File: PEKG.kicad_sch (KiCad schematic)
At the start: 57 parts, among them J1 USB_C_Receptacle, J2 Klema, J3 Klema, U1 TL072, U10 74LVC1G125, U11 74LVC1G125, U2 TL072, U3 TL072, U4 74LVC2G74, U5 TS5A63157DBV, U6 TS5A63157DBV, U7 TS5A63157DBV, U9 74LVC1G125

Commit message: Changed input opamps to NCS.
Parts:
- removed U1, U2: TL072, Package_SO:SOIC-8_3.9x4.9mm_P1.27mm, symbol Amplifier_Operational:TL072
- added U12, U8: NCS21802DMR2G, Package_SO:OnSemi_Micro8, symbol voltmeter_lib:NCS21802DMR2G
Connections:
- net BUFFERS_OUTPUT: now also U12.1
- net COMMON_INPUT_LEVEL: now also U12.6 (-)
- net GND: now also J1.A5 (CC1), J1.B5 (CC2), U12.5 (+)
- net VCC: now also U12.8 (V+), U8.8 (V+)
- net VEE: now also U12.4 (V-), U8.4 (V-)
- net at R7.1, R8.2: now also U12.2 (-)
- net at R6.1, R9.2: now also U12.3 (+)
- net at D2.3 (K), R11.1: now also U8.5 (+)
- net at C15.1, R2.1, R3.2: now also U8.6 (-)
- net at C15.2, R3.1, R5.1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: now also U8.7
- net at C16.2, R1.1, R2.2: now also U8.2 (-)
- net at C16.1, R1.2, R4.2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: now also U8.1
- net at D1.3 (K), R10.1: now also U8.3 (+)
- net at R13.1: now also U12.7
- no-connect marks 15 -> 13
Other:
- note added: "Implementiraj neki invertujući prekidački konverter za -5V rail. Možda switched capacitor."
- note added: "https://www.usb.org/sites/default/files/USB%20Type-C%20Spec%20R2.0%20-%20August%202019.pdf"

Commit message: Added stages, todos.
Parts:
- removed U3: TL072, Package_SO:SOIC-8_3.9x4.9mm_P1.27mm, symbol Amplifier_Operational:TL072
- added C21, C22, C23: 10u, Capacitor_SMD:C_0603_1608Metric_Pad1.08x0.95mm_HandSolder, symbol Device:C
- added C24, C25: 10n, Capacitor_SMD:C_0603_1608Metric_Pad1.08x0.95mm_HandSolder, symbol Device:C
- added C26: 100n, Capacitor_SMD:C_0603_1608Metric_Pad1.08x0.95mm_HandSolder, symbol Device:C
- added C27: 1u, Capacitor_SMD:C_0603_1608Metric_Pad1.08x0.95mm_HandSolder, symbol Device:C
- added R17, R24: 100k, Resistor_SMD:R_0603_1608Metric_Pad0.98x0.95mm_HandSolder, symbol Device:R
- added R25: 190k, Resistor_SMD:R_0603_1608Metric_Pad0.98x0.95mm_HandSolder, symbol Device:R
- added R26, R27, R30, R31: 10k, Resistor_SMD:R_0603_1608Metric_Pad0.98x0.95mm_HandSolder, symbol Device:R
- added R28, R29: 20k, Resistor_SMD:R_0603_1608Metric_Pad0.98x0.95mm_HandSolder, symbol Device:R
- added U13, U14: NCS21802DMR2G, Package_SO:OnSemi_Micro8, symbol voltmeter_lib:NCS21802DMR2G
- C15, C16: now not fitted
- C7: value 10u -> 100n
- R1, R3: value 1k -> 20k
- R15, R16, R18, R23: value 1k -> 100k
- R2: value 1k -> 10k
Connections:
- net COMMON_OUTPUT_LEVEL is gone; now on net DC_COMPENSATION: R9.1
- net OUTPUT is gone; now on net VCC: R18.2
- net DC_COMPENSATION: now also R16.1, C22.1, U13.1; no longer C7.1, R16.2
- net GND: now also C7.2, C26.1, R24.1; no longer R23.1
- net VCC: now also C7.1, C27.1, R28.2, U13.8 (V+), U14.8 (V+)
- net VEE: now also C26.2, C27.2, U13.4 (V-), U14.4 (V-)
- net TOP: now reaches C16.1, R1.2, R4.2, R6.2, U8.1
- net TOP: now also R15.2
- net BOTTOM: now reaches C15.2, R3.1, R5.1, R7.2, U8.7
- net BOTTOM: now also R14.2
- net at R23.2: now also C23.2, U13.6 (-); no longer R18.1
- net at R14.1: now also R16.2, C22.2, U13.2 (-); no longer C7.2
- net at R15.1: now also C21.1, R17.1, U13.3 (+); no longer R16.1
- net BUFFERS_OUTPUT renamed GAIN_5_OUTPUT
- net GAIN_5_OUTPUT: now also U14.3 (+); no longer R14.2, R15.2
- new net: C24.2, R25.2, R26.1, U14.2 (-)
- new net: R30.1, R31.1, U14.5 (+)
- new net: C25.2, R27.2, R28.1, R29.1, U14.6 (-)
- new net: R18.1, R24.2, U13.5 (+)
- new net 2.5V: C21.2, C23.1, R17.2, R23.1, R26.2, R29.2, R31.2, U13.7
- new net GAIN_100_OUTPUT: C24.1, R25.1, R30.2, U14.1
- new net LEVELED_OUTPUT: C25.1, R27.1, U14.7
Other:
- note added: "DODATI NOTCH FILTER"
- note added: "DOUBLE CHECK VREDNOSTI"
- note added: "MOŽDA DODATI JEFTINIJI OPAMP NAKOG GAIN-A"
- note added: "PRERAČUNATI PROPUSNE OPSEGE"
- note removed: "Implementiraj neki invertujući prekidački konverter za -5V rail. Možda switched capacitor."
- moved on the sheet: C10, R14

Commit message: Minor update.
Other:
- note added: "Gain to 100, changing the common mode point"
- moved on the sheet: C14, C24, C25, C26, C27, C7, J1, J2, J3, R25, R26, R27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

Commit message: Little PCB modifications.
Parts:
- removed J2, J3: Klema, TerminalBlock:TerminalBlock_MaiXu_MX126-5.0-02P_1x02_P5.00mm, symbol Connector:Screw_Terminal_01x02
- added H1, H2, H3, H4: MountingHole, MountingHole:MountingHole_3.2mm_M3_ISO14580_Pad_TopBottom, symbol Mechanical:MountingHole
- added J2: AudioJack3, PEKG:Jack_3.5mm_CUI_SJ1-3523N_Horizontal, symbol Connector_Audio:AudioJack3
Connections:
- net RIGHT_LEG_DRIVE: now also J2.T
- net NEGATIVE_INPUT renamed RIGHT_ARM
- net RIGHT_ARM: now also J2.S
- net POSITIVE_INPUT renamed LEFT_ARM
- net LEFT_ARM: now also J2.R

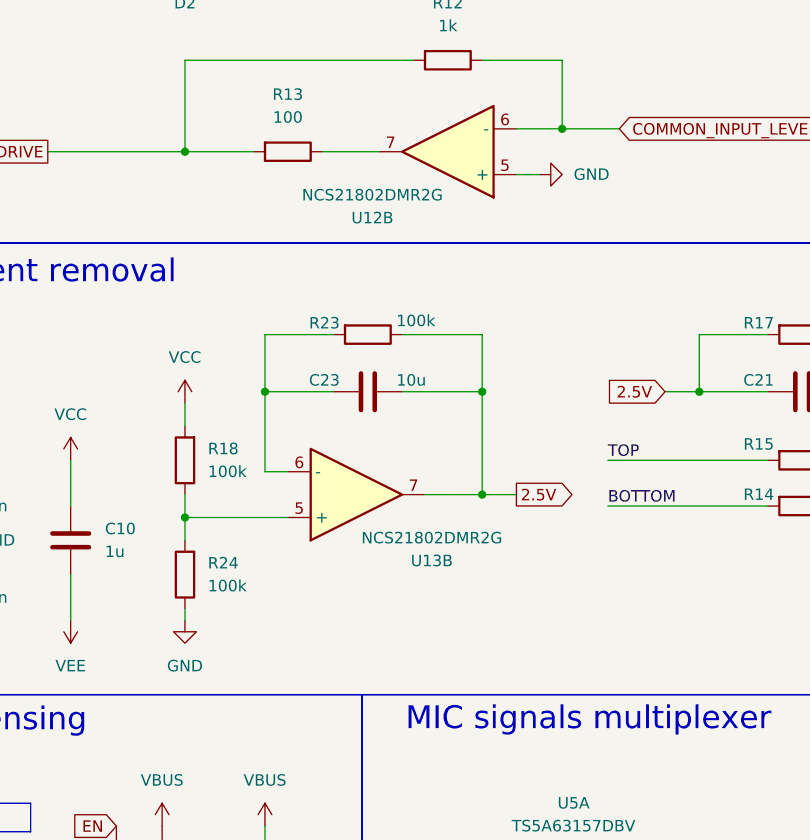
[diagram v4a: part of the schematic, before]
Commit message: Tad saner schematic.
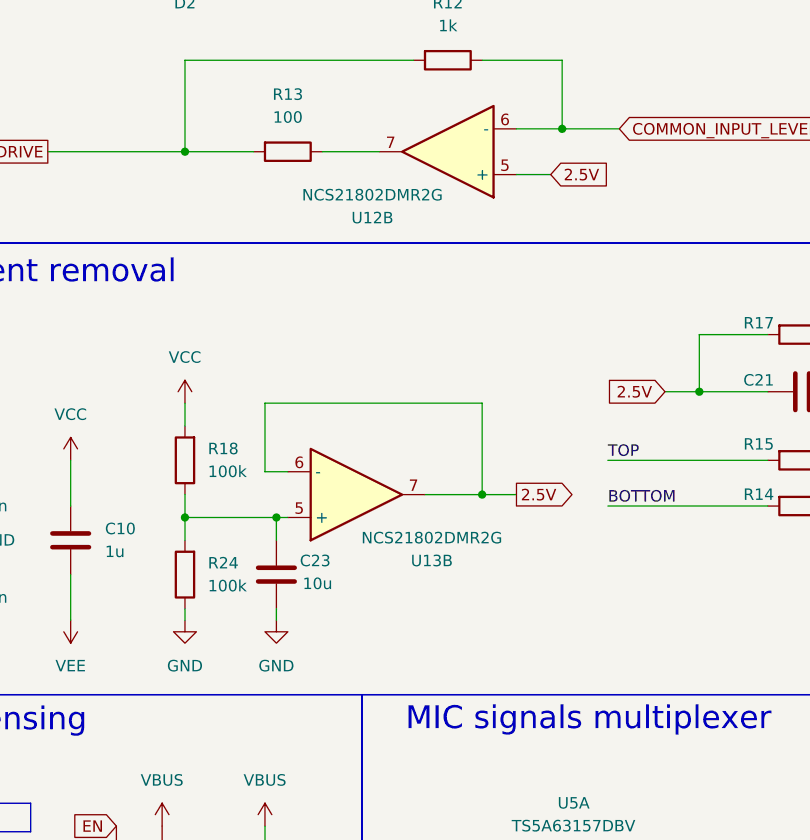
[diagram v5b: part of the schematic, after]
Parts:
- removed R23: 100k, Resistor_SMD:R_0603_1608Metric_Pad0.98x0.95mm_HandSolder, symbol Device:R
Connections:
- net 2.5V: now also U12.5 (+), U13.6 (-); no longer C23.1
- net GND: now also C23.2; no longer U12.5 (+)
- net at R18.1, R24.2, U13.5 (+): now also C23.1
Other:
- moved on the sheet: C23
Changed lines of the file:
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@@
 	)
 	(junction
-		(at 67.31 137.16)
-		(diameter 0)
-		(color 0 0 0 0)
-	)
-	(junction
 		(at 33.02 58.42)
 		(diameter 0)
@@
 	)
 	(junction
-		(at 58.42 64.77)
+		(at 68.58 151.13)
 		(diameter 0)
 		(color 0 0 0 0)
 	)
 	(junction
-		(at 82.55 64.77)
+		(at 58.42 64.77)
 		(diameter 0)
 		(color 0 0 0 0)
 	)
 	(junction
-		(at 91.44 39.37)
+		(at 82.55 64.77)
 		(diameter 0)
 		(color 0 0 0 0)
 	)
 	(junction
-		(at 91.44 137.16)
+		(at 91.44 39.37)
 		(diameter 0)
 		(color 0 0 0 0)
@@
 	(wire
 		(pts
-			(xy 91.44 137.16) (xy 91.44 148.59)
-		)
-		(stroke
-			(width 0)
-			(type default)
-		)
-	)
-	(wire
-		(pts
 			(xy 133.35 259.08) (xy 133.35 260.35)
 		)
@@
 	(wire
 		(pts
-			(xy 58.42 151.13) (xy 69.85 151.13)
+			(xy 58.42 151.13) (xy 68.58 151.13)
 		)
 		(stroke
@@
 	(wire
 		(pts
-			(xy 82.55 130.81) (xy 91.44 130.81)
-		)
-		(stroke
-			(width 0)
-			(type default)
-		)
-	)
-	(wire
-		(pts
 			(xy 161.29 162.56) (xy 161.29 156.21)
 		)
@@
 	(wire
 		(pts
-			(xy 82.55 137.16) (xy 91.44 137.16)
-		)
-		(stroke
-			(width 0)
-			(type default)
-		)
-	)
-	(wire
-		(pts
 			(xy 137.16 162.56) (xy 137.16 156.21)
 		)
@@
 	(wire
 		(pts
-			(xy 148.59 251.46) (xy 148.59 252.73)
+			(xy 68.58 151.13) (xy 69.85 151.13)
 		)
 		(stroke
@@
 	(wire
 		(pts
-			(xy 265.43 91.44) (xy 259.08 91.44)
+			(xy 148.59 251.46) (xy 148.59 252.73)
 		)
 		(stroke
@@
 	(wire
 		(pts
-			(xy 95.25 107.95) (xy 100.33 107.95)
+			(xy 265.43 91.44) (xy 259.08 91.44)
 		)
 		(stroke
@@
 	(wire
 		(pts
-			(xy 67.31 130.81) (xy 67.31 137.16)
+			(xy 95.25 107.95) (xy 100.33 107.95)
 		)
 		(stroke
@@
 	(wire
 		(pts
+			(xy 68.58 161.29) (xy 68.58 162.56)
+		)
+		(stroke
+			(width 0)
+			(type default)
+		)
+	)
+	(wire
+		(pts
 			(xy 105.41 58.42) (xy 105.41 64.77)
 		)
@@
 	(wire
 		(pts
-			(xy 74.93 137.16) (xy 67.31 137.16)
-		)
-		(stroke
-			(width 0)
-			(type default)
-		)
-	)
-	(wire
-		(pts
 			(xy 166.37 93.98) (xy 166.37 99.06)
 		)
@@
 	(wire
 		(pts
-			(xy 91.44 137.16) (xy 91.44 130.81)
+			(xy 91.44 138.43) (xy 91.44 148.59)
 		)
 		(stroke
@@
 	(wire
 		(pts
-			(xy 97.79 113.03) (xy 95.25 113.03)
+			(xy 68.58 153.67) (xy 68.58 151.13)
+		)
+		(stroke
+			(width 0)
+			(type default)
+		)
+	)
+	(wire
+		(pts
+			(xy 99.06 113.03) (xy 95.25 113.03)
 		)
 		(stroke
@@
 	(wire
 		(pts
-			(xy 67.31 137.16) (xy 67.31 146.05)
+			(xy 67.31 138.43) (xy 67.31 146.05)
 		)
 		(stroke
@@
 	(wire
 		(pts
-			(xy 67.31 130.81) (xy 74.93 130.81)
+			(xy 67.31 138.43) (xy 91.44 138.43)
 		)
 		(stroke
@@
 			"pKTE03MUarV68eLF4eHh07G4wZIlS1QqlS97CA4OXrJkieTXysPJCgAAQcDRMQCAICDHAACCgBwD"
 			"AAgCcgwAIAjIMQCAICDHAACCgBwDAAgCcgwAIAjIMQCAICDHAACCgBwDAAgCcgwAIAjIMQCAICDH"
-			"AACCgBwDAAgCcgwAIAjIMQCAICDHAACC8P9FoxsOaeCU/wAAAABJRU5ErkJggg=="
+			"AACCgBwDAAgCcgwAIAjIMQCAICDHAACC8P9FoxsOaeCU/wAAAABJRU5ErkJgggAAAAAAAAAAAAAA"
+			"AAAAAAAAAAAAAAAAAAAAAAAAAAAAAAAAAAAAAAAAAAAAAAAAAAAAAAAAAAAAAAAAAAAAAAAAAAAA"
+			"AAAAAAAAAAAAAAAAAAAAAAAAAAAAAAAAAAAAAAAAAAAAAAAAAAAAAAAAAAAAAAAAAAAAAAAAAAAA"
+			"AAAAAAAAAAAAAAAAAAAAAAAAAAAAAAAAAAAAAAAAAAAAAAAAAAAAAAAAAAAAAAAAAAAAAAAAAAAA"
+			"AAAAAAAAAAAAAAAAAAAAAAAAAAAAAAAAAAAAAAAAAAAAAAAAAAAAAAAAAAAAAAAAAAAAAAAAAAAA"
+			"AAAAAAAAAAAAAAAAAAAAAAAAAAAAAAAAAAAAAAAAAAAAAAAAAAAAAAAAAAAAAAAAAAAAAAAAAAAA"
+			"AAAAAAAAAAAAAAAAAAAAAAAAAAAAAAAAAAAAAAAAAAAAAAAAAAAAAAAAAAAAAAAAAAAAAAAAAAAA"
+			"AAAAAAAAAAAAAAAAAAAAAAAAAAAAAAAAAAAAAAAAAAAAAAAAAAAAAAAAAAAAAAAAAAAAAAAAAAAA"
+			"AAAAAAAAAAAAAAAAAAAAAAAAAAAAAAAAAAAAAAAAAAAAAAAAAAAAAAAAAAAAAAAAAAAAAAAAAAAA"
+			"AAAAAAAAAAAAAAAAAAAAAAAAAAAAAAAAAAAAAAAAAAAAAAAAAAAAAAAAAAAAAAAAAAAAAAAAAAAA"
+			"AAAAAAAAAAAAAAAAAAAAAAAAAAAAAAAAAAAAAAAAAAAAAAAAAAAAAAAAAAAAAAAAAAAAAAAAAAAA"
+			"AAAAAAAAAAAAAAAAAAAAAAAAAAAAAAAAAAAAAAAAAAAAAAAAAAAAAAAAAAAAAAAAAAAAAAAAAAAA"
+			"AAAAAAAAAAAAAAAAAAAAAAAAAAAAAAAAAAAAAAAAAAAAAAAAAAAAAAAAAAAAAAAAAAAAAAAAAAAA"
+			"AAAAAAAAAAAAAAAAAAAAAAAAAAAAAAAAAAAAAAAAAAAAAAAAAAAAAAAAAAAAAAAAAAAAAAAAAAAA"
+			"AAAAAAAAAAAAAAAAAAAAAAAAAAAAAAAAAAAAAAAAAAAAAAAAAAAAAAAAAAAAAAAAAAAAAAAAAAAA"
+			"AAAAAAAAAAAAAAAAAAAAAAAAAAAAAAAAAAAAAAAAAAAAAAAAAAAAAAAAAAAAAAAAAAAAAAAAAAAA"
+			"AAAAAAAAAAAAAAAAAAAAAAAAAAAAAAAAAAAAAAAAAAAAAAAAAAAAAAAAAAAAAAAAAAAAAAAAAAAA"
+			"AAAAAAAAAAAAAAAAAAAAAAAAAAAAAAAAAAAAAAAAAAAAAAAAAAAAAAAAAAAAAAAAAAAAAAAAAAAA"
+			"AAAAAAAAAAAAAAAAAAAAAAAAAAAAAAAAAAAAAAAAAAAAAAAAAAAAAAAAAAAAAA=="
 		)
 	)
@@
 	(global_label "2.5V"
 		(shape input)
+		(at 99.06 113.03 0)
+		(fields_autoplaced yes)
+		(effects
+			(font
+				(size 1.27 1.27)
+			)
+			(justify left)
+		)
+		(property "Intersheetrefs" "${INTERSHEET_REFS}"
+			(at 106.1576 113.03 0)
+			(effects
+				(font
+					(size 1.27 1.27)
+				)
+				(justify left)
+				(hide yes)
+			)
+		)
+	)
+	(global_label "2.5V"
+		(shape input)
 		(at 217.17 80.01 180)
 		(fields_autoplaced yes)
@@
 	)
 	(symbol
-		(lib_id "Device:R")
-		(at 78.74 130.81 270)
-		(unit 1)
-		(exclude_from_sim no)
-		(in_bom yes)
-		(on_board yes)
-		(dnp no)
-		(property "Reference" "R23"
-			(at 73.914 129.54 90)
-			(effects
-				(font
-					(size 1.27 1.27)
-				)
-			)
-		)
-		(property "Value" "100k"
-			(at 84.074 129.286 90)
-			(effects
-				(font
-					(size 1.27 1.27)
-				)
-			)
-		)
-		(property "Footprint" "Resistor_SMD:R_0603_1608Metric_Pad0.98x0.95mm_HandSolder"
-			(at 78.74 129.032 90)
-			(effects
-				(font
-					(size 1.27 1.27)
-				)
-				(hide yes)
-			)
-		)
-		(property "Datasheet" "~"
-			(at 78.74 130.81 0)
-			(effects
-				(font
-					(size 1.27 1.27)
-				)
-				(hide yes)
-			)
-		)
-		(property "Description" "Resistor"
-			(at 78.74 130.81 0)
-			(effects
-				(font
-					(size 1.27 1.27)
-				)
-				(hide yes)
-			)
-		)
-		(pin "2"
-		)
-		(pin "1"
-		)
-		(instances
-			(project "PEKG"
-				(path "/6b6ace37-3aeb-4177-8f53-de4683f890d9"
-					(reference "R23")
-					(unit 1)
-				)
-			)
-		)
-	)
-	(symbol
 		(lib_id "power:VCC")
 		(at 17.78 146.05 0)
@@
 	)
 	(symbol
-		(lib_id "power:GND")
-		(at 97.79 113.03 90)
-		(unit 1)
-		(exclude_from_sim no)
-		(in_bom yes)
-		(on_board yes)
-		(dnp no)
-		(fields_autoplaced yes)
-		(property "Reference" "#PWR022"
-			(at 104.14 113.03 0)
-			(effects
-				(font
-					(size 1.27 1.27)
-				)
-				(hide yes)
-			)
-		)
-		(property "Value" "GND"
-			(at 101.6 113.0299 90)
-			(effects
-				(font
-					(size 1.27 1.27)
-				)
-				(justify right)
-			)
-		)
-		(property "Footprint" ""
-			(at 97.79 113.03 0)
-			(effects
-				(font
-					(size 1.27 1.27)
-				)
-				(hide yes)
-			)
-		)
-		(property "Datasheet" ""
-			(at 97.79 113.03 0)
-			(effects
-				(font
-					(size 1.27 1.27)
-				)
-				(hide yes)
-			)
-		)
-		(property "Description" "Power symbol creates a global label with name \"GND\" , ground"
-			(at 97.79 113.03 0)
-			(effects
-				(font
-					(size 1.27 1.27)
-				)
-				(hide yes)
-			)
-		)
-		(pin "1"
-		)
-		(instances
-			(project "EEG"
-				(path "/6b6ace37-3aeb-4177-8f53-de4683f890d9"
-					(reference "#PWR022")
-					(unit 1)
-				)
-			)
-		)
-	)
-	(symbol
 		(lib_id "power:VCC")
 		(at 66.04 29.21 270)
@@
 	(symbol
 		(lib_id "Device:C")
-		(at 78.74 137.16 270)
-		(mirror x)
+		(at 68.58 157.48 0)
+		(mirror y)
 		(unit 1)
 		(exclude_from_sim no)
@@
 		(dnp no)
 		(property "Reference" "C23"
-			(at 73.914 135.89 90)
+			(at 72.898 155.956 0)
 			(effects
 				(font
@@
 		)
 		(property "Value" "10u"
-			(at 83.566 135.89 90)
+			(at 73.152 158.496 0)
 			(effects
 				(font
@@
 		)
 		(property "Footprint" "Capacitor_SMD:C_0603_1608Metric_Pad1.08x0.95mm_HandSolder"
-			(at 74.93 136.1948 0)
+			(at 67.6148 161.29 0)
 			(effects
 				(font
@@
 		)
 		(property "Datasheet" "~"
-			(at 78.74 137.16 0)
+			(at 68.58 157.48 0)
 			(effects
 				(font
@@
 		)
 		(property "Description" "Unpolarized capacitor"
-			(at 78.74 137.16 0)
+			(at 68.58 157.48 0)
 			(effects
 				(font
@@
 					(unit 1)
 				)
+			)
+		)
+	)
+	(symbol
+		(lib_id "power:GND")
+		(at 68.58 162.56 0)
+		(unit 1)
+		(exclude_from_sim no)
+		(in_bom yes)
+		(on_board yes)
+		(dnp no)
+		(fields_autoplaced yes)
+		(property "Reference" "#PWR081"
+			(at 68.58 168.91 0)
+			(effects
+				(font
+					(size 1.27 1.27)
+				)
+				(hide yes)
+			)
+		)
+		(property "Value" "GND"
+			(at 68.58 167.64 0)
+			(effects
+				(font
+					(size 1.27 1.27)
+				)
+			)
+		)
+		(property "Footprint" ""
+			(at 68.58 162.56 0)
+			(effects
+				(font
+					(size 1.27 1.27)
+				)
+				(hide yes)
+			)
+		)
+		(property "Datasheet" ""
+			(at 68.58 162.56 0)
+			(effects
+				(font
+					(size 1.27 1.27)
+				)
+				(hide yes)
+			)
+		)
+		(property "Description" "Power symbol creates a global label with name \"GND\" , ground"
+			(at 68.58 162.56 0)
+			(effects
+				(font
+					(size 1.27 1.27)
+				)
+				(hide yes)
+			)
+		)
+		(pin "1"
+		)
+		(instances
+			(project "PEKG"
+				(path "/6b6ace37-3aeb-4177-8f53-de4683f890d9"
+					(reference "#PWR081")
+					(unit 1)
+				)

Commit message: Newwww
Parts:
- R12: value 1k -> 100k -> inf
- R13: value 100 -> 1
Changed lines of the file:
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@@
 			"AAAAAAAAAAAAAAAAAAAAAAAAAAAAAAAAAAAAAAAAAAAAAAAAAAAAAAAAAAAAAAAAAAAAAAAAAAAA"
 			"AAAAAAAAAAAAAAAAAAAAAAAAAAAAAAAAAAAAAAAAAAAAAAAAAAAAAAAAAAAAAAAAAAAAAAAAAAAA"
+			"AAAAAAAAAAAAAAAAAAAAAAAAAAAAAAAAAAAAAAAAAAAAAAAAAAAAAAAAAAAAAAAAAAAAAAAAAAAA"
+			"AAAAAAAAAAAAAAAAAAAAAAAAAAAAAAAAAAAAAAAAAAAAAAAAAAAAAAAAAAAAAAAAAAAAAAAAAAAA"
+			"AAAAAAAAAAAAAAAAAAAAAAAAAAAAAAAAAAAAAAAAAAAAAAAAAAAAAAAAAAAAAAAAAAAAAAAAAAAA"
+			"AAAAAAAAAAAAAAAAAAAAAAAAAAAAAAAAAAAAAAAAAAAAAAAAAAAAAAAAAAAAAAAAAAAAAAAAAAAA"
+			"AAAAAAAAAAAAAAAAAAAAAAAAAAAAAAAAAAAAAAAAAAAAAAAAAAAAAAAAAAAAAAAAAAAAAAAAAAAA"
+			"AAAAAAAAAAAAAAAAAAAAAAAAAAAAAAAAAAAAAAAAAAAAAAAAAAAAAAAAAAAAAAAAAAAAAAAAAAAA"
+			"AAAAAAAAAAAAAAAAAAAAAAAAAAAAAAAAAAAAAAAAAAAAAAAAAAAAAAAAAAAAAAAAAAAAAAAAAAAA"
+			"AAAAAAAAAAAAAAAAAAAAAAAAAAAAAAAAAAAAAAAAAAAAAAAAAAAAAAAAAAAAAAAAAAAAAAAAAAAA"
+			"AAAAAAAAAAAAAAAAAAAAAAAAAAAAAAAAAAAAAAAAAAAAAAAAAAAAAAAAAAAAAAAAAAAAAAAAAAAA"
+			"AAAAAAAAAAAAAAAAAAAAAAAAAAAAAAAAAAAAAAAAAAAAAAAAAAAAAAAAAAAAAAAAAAAAAAAAAAAA"
+			"AAAAAAAAAAAAAAAAAAAAAAAAAAAAAAAAAAAAAAAAAAAAAAAAAAAAAAAAAAAAAAAAAAAAAAAAAAAA"
+			"AAAAAAAAAAAAAAAAAAAAAAAAAAAAAAAAAAAAAAAAAAAAAAAAAAAAAAAAAAAAAAAAAAAAAAAAAAAA"
+			"AAAAAAAAAAAAAAAAAAAAAAAAAAAAAAAAAAAAAAAAAAAAAAAAAAAAAAAAAAAAAAAAAAAAAAAAAAAA"
+			"AAAAAAAAAAAAAAAAAAAAAAAAAAAAAAAAAAAAAAAAAAAAAAAAAAAAAAAAAAAAAAAAAAAAAAAAAAAA"
+			"AAAAAAAAAAAAAAAAAAAAAAAAAAAAAAAAAAAAAAAAAAAAAAAAAAAAAAAAAAAAAAAAAAAAAAAAAAAA"
+			"AAAAAAAAAAAAAAAAAAAAAAAAAAAAAAAAAAAAAAAAAAAAAAAAAAAAAAAAAAAAAAAAAAAAAAAAAAAA"
+			"AAAAAAAAAAAAAAAAAAAAAAAAAAAAAAAAAAAAAAAAAAAAAAAAAAAAAAAAAAAAAAAAAAAAAAAAAAAA"
+			"AAAAAAAAAAAAAAAAAAAAAAAAAAAAAAAAAAAAAAAAAAAAAAAAAAAAAAAAAAAAAAAAAAAAAAAAAAAA"
 			"AAAAAAAAAAAAAAAAAAAAAAAAAAAAAAAAAAAAAAAAAAAAAAAAAAAAAAAAAAAAAA=="
 		)
@@
 			)
 		)
-		(property "Value" "100"
+		(property "Value" "1"
 			(at 69.85 106.68 90)
 			(effects
@@
 			)
 		)
-		(property "Value" "1k"
+		(property "Value" "100k -> inf"
 			(at 87.63 96.52 90)
 			(effects

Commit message: Updated values added note.
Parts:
- R4, R5, R6, R7, R8, R9: value 1k -> 10k
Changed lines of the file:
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@@
 		)
 	)
+	(text_box "R8 i R9 ne sme biti prevelik, \nprevelik gain će zasiti opamp"
+		(exclude_from_sim no)
+		(at 139.7 43.18 0)
+		(size 31.75 5.08)
+		(margins 0.9525 0.9525 0.9525 0.9525)
+		(stroke
+			(width 0)
+			(type solid)
+		)
+		(fill
+			(type none)
+		)
+		(effects
+			(font
+				(size 1.27 1.27)
+			)
+			(justify left top)
+		)
+	)
 	(junction
 		(at 91.44 77.47)
@@
 			"AAAAAAAAAAAAAAAAAAAAAAAAAAAAAAAAAAAAAAAAAAAAAAAAAAAAAAAAAAAAAAAAAAAAAAAAAAAA"
 			"AAAAAAAAAAAAAAAAAAAAAAAAAAAAAAAAAAAAAAAAAAAAAAAAAAAAAAAAAAAAAAAAAAAAAAAAAAAA"
-			"AAAAAAAAAAAAAAAAAAAAAAAAAAAAAAAAAAAAAAAAAAAAAAAAAAAAAAAAAAAAAA=="
+			"AAAAAAAAAAAAAAAAAAAAAAAAAAAAAAAAAAAAAAAAAAAAAAAAAAAAAAAAAAAAAAAAAAAAAAAAAAAA"
+			"AAAAAAAAAAAAAAAAAAAAAAAAAAAAAAAAALgHyWmDfwAAAQDpBwAAAAAAAAAAAAAAAAAAAAAAAAAA"
+			"qNf0E4N/AADc+zYkYmZJ1awlY+Bitfp2MAAAAAAAAAAAWekHAAAAAAAAAQDOAwAAAAAAAAAAAAAA"
+			"AAAAAAAAAAAAAAAAAAAAYK/pBwAAAAAAAAAAAAAAAAAAAAAAAAAAwJ/pBwAAAADAn+kHAAAAAAAA"
+			"AAAAAAAAGKDpBwAAAAABAAAAAAAAAAAAAAAAAAAAAAAAAAAAAAAAAIA/AAAAAAAAAAAAAAAAAAAA"
+			"AAAAAAAA5ekHAAAAAFig6QcAAAAAAQAAAAAAAAAAAAAAAAAAAAAAAAAAAAAAAACAPwAAAAAAAAAA"
+			"AAAAAAAAAAAAAAAAgNHuE4N/AAB4oOkHAAAAAAAAAAAAAAAAAAAAAAAAAABwoOkHAAAAAAAAAAAA"
+			"AAAAAAAAAAAAAADAS+kHAAAAADgAAAAAAAAAOAAAAAAAAABa4ekHAAAAAAAAAAAAAAAAAAAAAAAA"
+			"AADgVukHAAAAADgAAAAAAAAAOAAAAAAAAAAAAAAAAAAAAAAAAAAAAAAAAAAAAAAAAAAAAAAAAAAA"
+			"ADAwuRODfwAAGKHpBwAAAAAAAAAAAAAAAAAAAAAAAAAAAAAAAAAAAAAAAAAAAAAAAAAAAAAAAAAA"
+			"AAAAAAAAAAAAAAAAAAAAAAAAAAAAAAAAAAAAAAAAAAAAAAAAAAAAAAAAAAAAAAAA8QUAAAAAAAAA"
+			"AAAAAAAAAOBWpQcAAAAA4FalBwAAAADgVqUHAAAAAAEAAAAAAAAAAAAAAAAAAAAAAAAAAAAAAAAA"
+			"AAAAgFZAAAAAAAAA8D8AAAAAAAAAAAAAAAAAAAAAAAAAAAAAAAAAAAAAAAAAAAAAAAAAAAAAAAAB"
+			"AJwxAACcMQAAAAAAAAAAAAAAAAAACKLpBwAAAAAAAAAAAAAAAAAAAACDfwAAAAAAgAAAAAAAAAAA"
+			"AAAAAAAAAAAAAAAAINAPAOh2CgACAAAAg38AAPBF6QcAAAAACQAAAAAAAAAJAAAAAAAAAECi6QcA"
+			"AAAAAAAAAAAAAAAAAAAAAAAAAAABAAABAAAAAAAAAAAAAAAAAAAAAAAAAAAAAAAAAAAAAAAAAAAA"
+			"AAAAAAAAAAAAAAAAAAAAAAAAAAAAAAAAAAAAAAAAAAAAALgHyWmDfwAAAQAAAAAAAAAAAAAAAAAA"
+			"AAAAAAAAAAAAqNf0E4N/AAD1VGaiicVBb6KhAIwLNEGaMAAAAAAAAAAAWekHAAAAAAAAAADOAwAA"
+			"AAAAAAAAAAAAoekHAAAAAAAAAAAAAAAAbwAAAAAAAAAAAAAAAAAAAAAAAAAAAA=="
 		)
 	)
@@
 			)
 		)
-		(property "Value" "1k"
+		(property "Value" "10k"
 			(at 146.05 73.66 90)
 			(effects
@@
 			)
 		)
-		(property "Value" "1k"
+		(property "Value" "10k"
 			(at 107.95 50.7999 0)
 			(effects
@@
 			)
 		)
-		(property "Value" "1k"
+		(property "Value" "10k"
 			(at 107.95 69.8499 0)
 			(effects
@@
 			)
 		)
-		(property "Value" "1k"
+		(property "Value" "10k"
 			(at 119.38 35.56 90)
 			(effects
@@
 			)
 		)
-		(property "Value" "1k"
+		(property "Value" "10k"
 			(at 119.38 73.66 90)
 			(effects
@@
 			)
 		)
-		(property "Value" "1k"
+		(property "Value" "10k"
 			(at 146.05 35.56 90)
 			(effects
